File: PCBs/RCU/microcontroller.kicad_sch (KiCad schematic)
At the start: 26 parts, among them J200 USB_C_Receptacle_USB2.0, J201 Conn_01x05, SW200 SW_SPDT, SW201 SW_Push, U200 STM32G0B1CBT6, Y200 Crystal

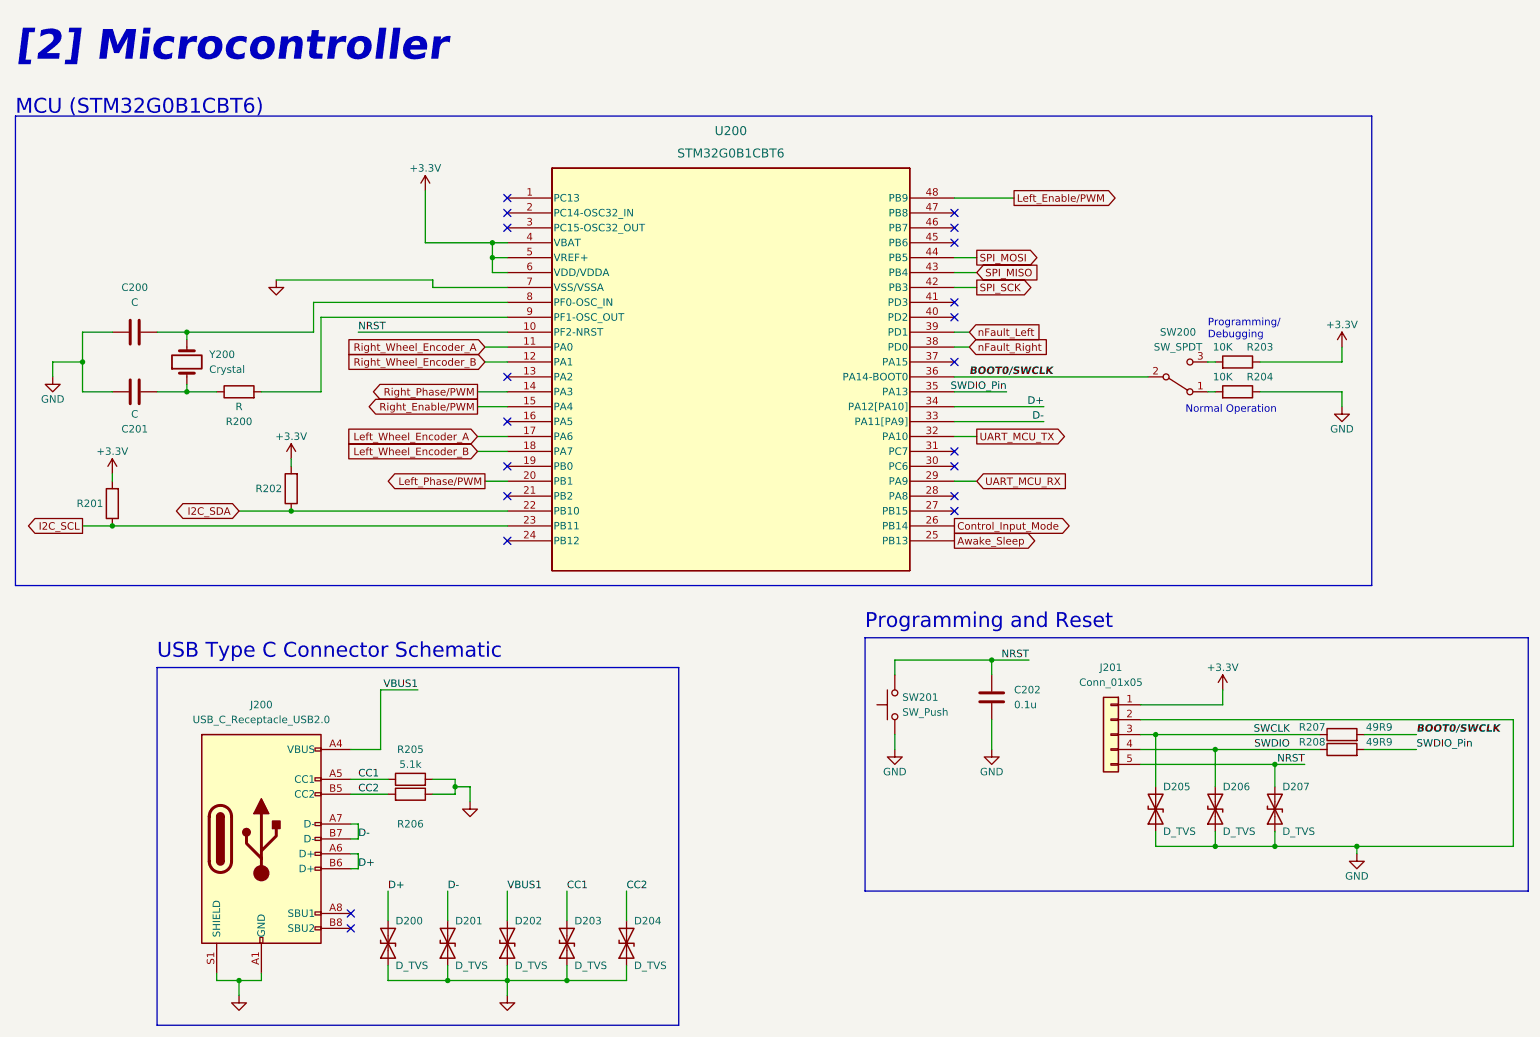
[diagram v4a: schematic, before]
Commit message: The shared SWCLK/BOOT0 pin has an internal pull-down resistor, and in the case where SWCLK is shared and are programming with SWD, just need NRST conncted to the STLink-V2 module
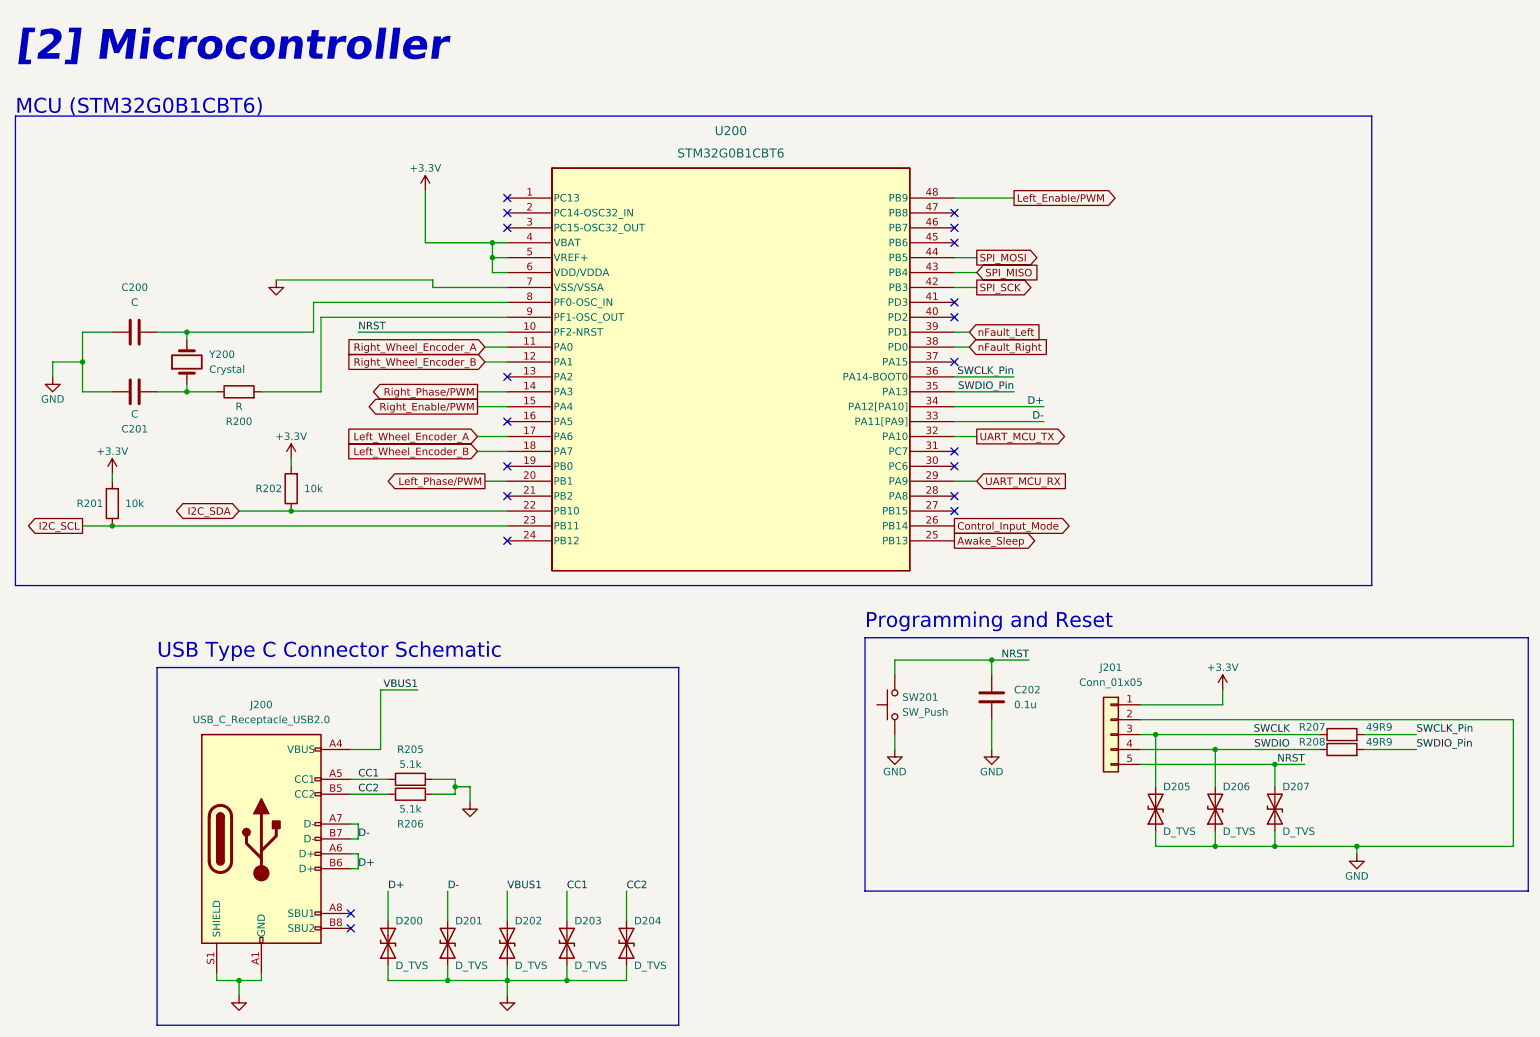
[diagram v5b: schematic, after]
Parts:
- removed R203, R204: 10K, symbol Device:R
- removed SW200: SW_SPDT, symbol Switch:SW_SPDT
- R201, R202: value (none) -> 10k
- R206: value (none) -> 5.1k
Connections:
- net BOOT0/SWCLK renamed SWCLK_Pin
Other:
- note removed: "Normal Operation"
- note removed: "Programming/ Debugging"
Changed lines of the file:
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@@
-    (stroke (width 0) (type default) (color 0 0 0 0))
-  )
-  (wire (pts (xy 245.11 82.55) (xy 245.11 80.01))
     (stroke (width 0) (type default) (color 0 0 0 0))
   )
@@
     (stroke (width 0) (type default) (color 0 0 0 0))
   )
-  (wire (pts (xy 223.52 80.01) (xy 222.25 80.01))
-    (stroke (width 0) (type default) (color 0 0 0 0))
-  )
   (wire (pts (xy 185.42 125.73) (xy 168.91 125.73))
     (stroke (width 0) (type default) (color 0 0 0 0))
@@
     (stroke (width 0) (type default) (color 0 0 0 0))
   )
+  (wire (pts (xy 179.07 77.47) (xy 189.23 77.47))
+    (stroke (width 0) (type default) (color 0 0 0 0))
+  )
   (wire (pts (xy 76.2 161.29) (xy 77.47 161.29))
     (stroke (width 0) (type default) (color 0 0 0 0))
@@
     (stroke (width 0) (type default) (color 0 0 0 0))
   )
-  (wire (pts (xy 245.11 74.93) (xy 231.14 74.93))
-    (stroke (width 0) (type default) (color 0 0 0 0))
-  )
   (wire (pts (xy 76.2 153.67) (xy 77.47 153.67))
     (stroke (width 0) (type default) (color 0 0 0 0))
   )
-  (wire (pts (xy 245.11 80.01) (xy 231.14 80.01))
-    (stroke (width 0) (type default) (color 0 0 0 0))
-  )
   (wire (pts (xy 93.98 147.32) (xy 96.52 147.32))
     (stroke (width 0) (type default) (color 0 0 0 0))
@@
     (stroke (width 0) (type default) (color 0 0 0 0))
   )
-  (wire (pts (xy 245.11 74.93) (xy 245.11 72.39))
-    (stroke (width 0) (type default) (color 0 0 0 0))
-  )
   (wire (pts (xy 182.88 62.23) (xy 179.07 62.23))
     (stroke (width 0) (type default) (color 0 0 0 0))
@@
     (stroke (width 0) (type default) (color 0 0 0 0))
   )
-  (wire (pts (xy 179.07 77.47) (xy 212.09 77.47))
-    (stroke (width 0) (type default) (color 0 0 0 0))
-  )
   (wire (pts (xy 100.33 54.61) (xy 88.9 54.61))
     (stroke (width 0) (type default) (color 0 0 0 0))
@@
     (stroke (width 0) (type default) (color 0 0 0 0))
   )
-  (wire (pts (xy 223.52 74.93) (xy 222.25 74.93))
-    (stroke (width 0) (type default) (color 0 0 0 0))
-  )
   (wire (pts (xy 97.79 90.17) (xy 102.87 90.17))
     (stroke (width 0) (type default) (color 0 0 0 0))
   )
-  (wire (pts (xy 187.96 80.01) (xy 179.07 80.01))
+  (wire (pts (xy 179.07 80.01) (xy 189.23 80.01))
     (stroke (width 0) (type default) (color 0 0 0 0))
   )
@@
   (wire (pts (xy 213.36 157.48) (xy 223.52 157.48))
     (stroke (width 0) (type default) (color 0 0 0 0))
-  )
-  (text "Normal Operation" (at 218.44 83.82 0)
-    (effects (font (size 1.27 1.27)) (justify left bottom))
   )
   (text "Programming and Reset" (at 163.83 120.65 0)
@@
     (effects (font (size 5.08 5.08) (thickness 1.016) bold italic) (justify left bottom))
   )
-  (text "Programming/\nDebugging\n" (at 222.25 71.12 0)
-    (effects (font (size 1.27 1.27)) (justify left bottom))
-  )
   (text "MCU (STM32G0B1CBT6)" (at 19.05 33.02 0)
     (effects (font (size 2.54 2.54)) (justify left bottom))
@@
     (effects (font (size 1.27 1.27)) (justify left bottom))
   )
-  (label "BOOT0{slash}SWCLK" (at 181.61 77.47 0)
-    (effects (font (size 1.27 1.27) (thickness 0.254) bold italic) (justify left bottom))
+  (label "SWCLK_Pin" (at 189.23 77.47 180)
+    (effects (font (size 1.27 1.27)) (justify right bottom))
   )
   (label "CC1" (at 113.03 165.1 0)
     (effects (font (size 1.27 1.27)) (justify left bottom))
   )
-  (label "BOOT0{slash}SWCLK" (at 257.81 138.43 0)
-    (effects (font (size 1.27 1.27) (thickness 0.254) bold italic) (justify left bottom))
+  (label "SWCLK_Pin" (at 257.81 138.43 0)
+    (effects (font (size 1.27 1.27)) (justify left bottom))
   )
   (label "VBUS1" (at 102.87 165.1 0)
@@
     (effects (font (size 1.27 1.27)) (justify left bottom))
   )
-  (label "SWDIO_Pin" (at 187.96 80.01 180)
+  (label "SWDIO_Pin" (at 189.23 80.01 180)
     (effects (font (size 1.27 1.27)) (justify right bottom))
   )
@@
     (in_bom yes) (on_board yes)
     (property "Reference" "R202" (id 0) (at 62.23 96.52 0))
-    (property "Value" "" (id 1) (at 69.85 96.52 0))
+    (property "Value" "10k" (id 1) (at 69.85 96.52 0))
     (property "Footprint" "" (id 2) (at 67.818 96.52 90)
       (effects (font (size 1.27 1.27)) hide)
@@
     (in_bom yes) (on_board yes)
     (property "Reference" "R206" (id 0) (at 86.36 153.67 90))
-    (property "Value" "" (id 1) (at 86.36 151.13 90))
+    (property "Value" "5.1k" (id 1) (at 86.36 151.13 90))
     (property "Footprint" "" (id 2) (at 86.36 150.368 90)
       (effects (font (size 1.27 1.27)) hide)
@@
     (pin "1")
     (pin "2")
-  )
-  (symbol (lib_id "power:GND") (at 245.11 82.55 0) (mirror y) (unit 1)
-    (in_bom yes) (on_board yes)
-    (property "Reference" "#PWR?" (id 0) (at 245.11 88.9 0)
-      (effects (font (size 1.27 1.27)) hide)
-    )
-    (property "Value" "GND" (id 1) (at 245.11 86.36 0))
-    (property "Footprint" "" (id 2) (at 245.11 82.55 0)
-      (effects (font (size 1.27 1.27)) hide)
-    )
-    (property "Datasheet" "" (id 3) (at 245.11 82.55 0)
-      (effects (font (size 1.27 1.27)) hide)
-    )
-    (pin "1")
   )
   (symbol (lib_id "power:GND") (at 247.65 158.75 0) (mirror y) (unit 1)
@@
     (in_bom yes) (on_board yes)
     (property "Reference" "R201" (id 0) (at 31.75 99.06 0))
-    (property "Value" "" (id 1) (at 39.37 99.06 0))
+    (property "Value" "10k" (id 1) (at 39.37 99.06 0))
     (property "Footprint" "" (id 2) (at 37.338 99.06 90)
       (effects (font (size 1.27 1.27)) hide)
@@
     (pin "1")
   )
-  (symbol (lib_id "Device:R") (at 227.33 80.01 270) (mirror x) (unit 1)
-    (in_bom yes) (on_board yes)
-    (property "Reference" "R204" (id 0) (at 231.14 77.47 90))
-    (property "Value" "10K" (id 1) (at 224.79 77.47 90))
-    (property "Footprint" "" (id 2) (at 227.33 81.788 90)
-      (effects (font (size 1.27 1.27)) hide)
-    )
-    (property "Datasheet" "~" (id 3) (at 227.33 80.01 0)
-      (effects (font (size 1.27 1.27)) hide)
-    )
-    (pin "1")
-    (pin "2")
-  )
   (symbol (lib_id "power:+3.3V") (at 66.04 91.44 0) (unit 1)
     (in_bom yes) (on_board yes)
@@
     )
     (property "Datasheet" "" (id 3) (at 66.04 91.44 0)
-      (effects (font (size 1.27 1.27)) hide)
-    )
-    (pin "1")
-  )
-  (symbol (lib_id "power:+3.3V") (at 245.11 72.39 0) (unit 1)
-    (in_bom yes) (on_board yes)
-    (property "Reference" "#PWR?" (id 0) (at 245.11 76.2 0)
-      (effects (font (size 1.27 1.27)) hide)
-    )
-    (property "Value" "+3.3V" (id 1) (at 245.11 68.58 0))
-    (property "Footprint" "" (id 2) (at 245.11 72.39 0)
-      (effects (font (size 1.27 1.27)) hide)
-    )
-    (property "Datasheet" "" (id 3) (at 245.11 72.39 0)
       (effects (font (size 1.27 1.27)) hide)
     )
@@
     (pin "1")
   )
-  (symbol (lib_id "Switch:SW_SPDT") (at 217.17 77.47 0) (mirror x) (unit 1)
-    (in_bom yes) (on_board yes) (fields_autoplaced)
-    (property "Reference" "SW200" (id 0) (at 217.17 69.85 0))
-    (property "Value" "SW_SPDT" (id 1) (at 217.17 72.39 0))
-    (property "Footprint" "" (id 2) (at 217.17 77.47 0)
-      (effects (font (size 1.27 1.27)) hide)
-    )
-    (property "Datasheet" "~" (id 3) (at 217.17 77.47 0)
-      (effects (font (size 1.27 1.27)) hide)
-    )
-    (pin "1")
-    (pin "2")
-    (pin "3")
-  )
-  (symbol (lib_id "Device:R") (at 227.33 74.93 270) (mirror x) (unit 1)
-    (in_bom yes) (on_board yes)
-    (property "Reference" "R203" (id 0) (at 231.14 72.39 90))
-    (property "Value" "10K" (id 1) (at 224.79 72.39 90))
-    (property "Footprint" "" (id 2) (at 227.33 76.708 90)
-      (effects (font (size 1.27 1.27)) hide)
-    )
-    (property "Datasheet" "~" (id 3) (at 227.33 74.93 0)
-      (effects (font (size 1.27 1.27)) hide)
-    )
-    (pin "1")
-    (pin "2")
-  )
   (symbol (lib_id "Device:C") (at 39.37 69.85 270) (unit 1)

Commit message: Add Diode to ensure USB2 only power Bluetooth module
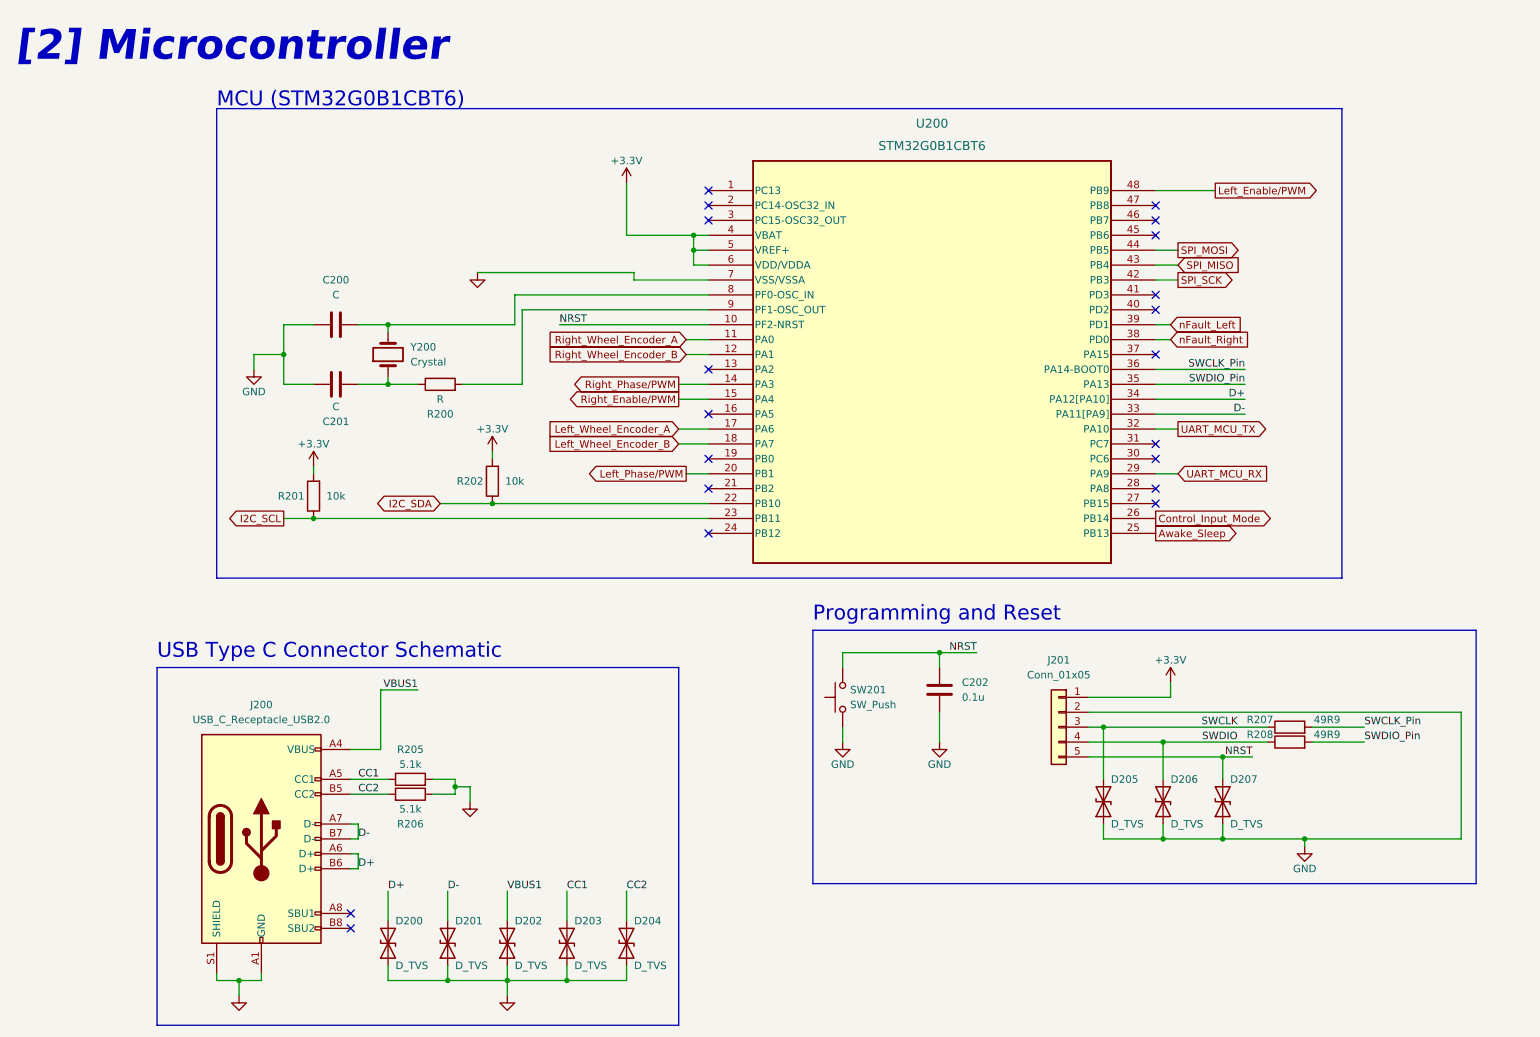
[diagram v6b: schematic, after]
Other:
- moved on the sheet: C200, C201, C202, D205, D206, D207, J201, R200, R201, R202, R207, R208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
